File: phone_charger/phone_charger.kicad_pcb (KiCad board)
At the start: 2 copper layers, 19 parts, among them J1 Conn_01x02, J2 UE27AC54100, U1 ADP2302

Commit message: placed components
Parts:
- D1, D2, F1, R1, R3, R4, R5, R6, R7: moved to B.Cu
- moved J2 35.9 mm to (101.1, 57.0)
- moved J1 25.9 mm to (90.1, 79.1), turned to 180 degrees
- moved R7 25.7 mm to (101.2, 57.1)
- moved D1 25.6 mm to (90.6, 73.9), turned to 90 degrees
- moved D2 20.8 mm to (97.4, 79.2), turned to 90 degrees
- moved R4 19.2 mm to (104.1, 60.0)
- moved C3 18.8 mm to (93.9, 70.3), turned to 270 degrees
- moved R3 18.6 mm to (99.3, 60.0)
- moved C4 18.6 mm to (97.5, 70.3), turned to 270 degrees
- moved R5 18.2 mm to (101.2, 63.3)
- moved L1 14.7 mm to (104.8, 64.6)
- moved R1 14.0 mm to (90.6, 54.2), turned to 270 degrees
- moved R6 13.9 mm to (105.8, 63.2)
- moved R2 12.6 mm to (97.5, 82.5)
- moved F1 11.5 mm to (98.3, 72.7), turned to 180 degrees
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
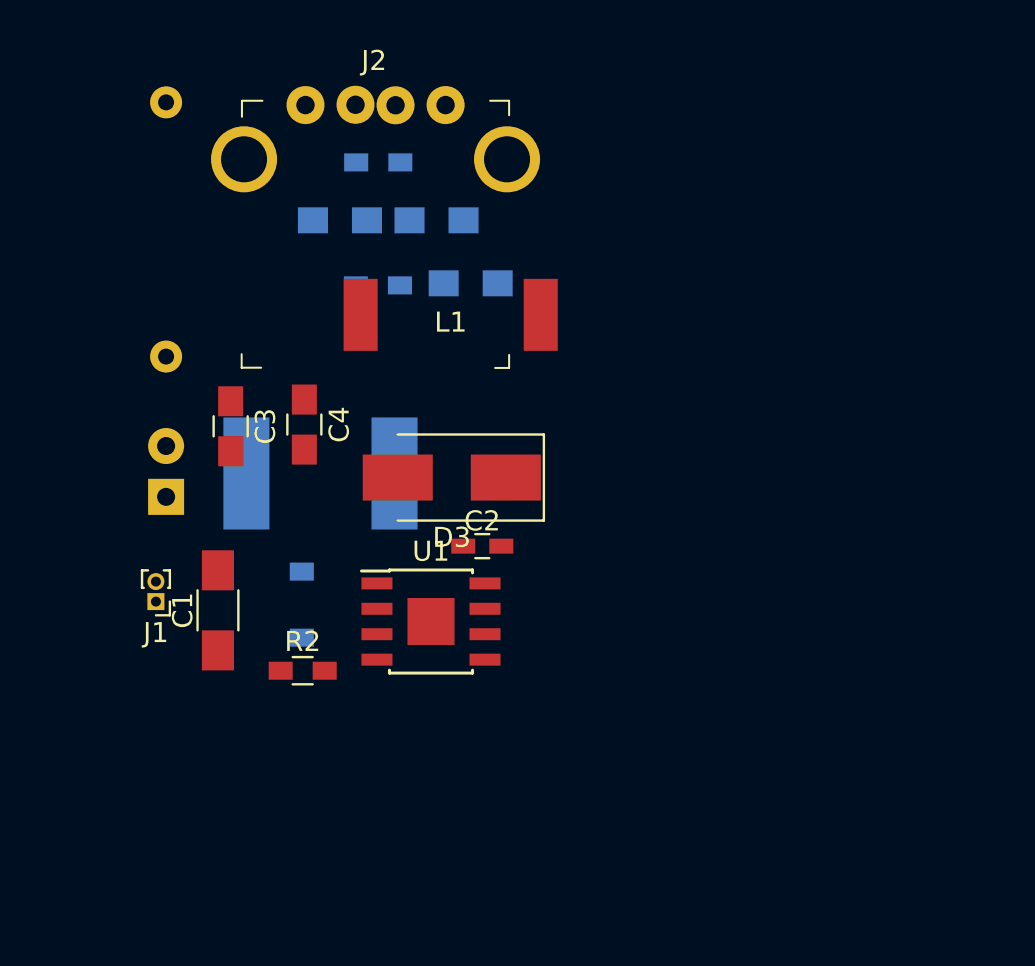
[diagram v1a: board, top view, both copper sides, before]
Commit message: laid out componenets onto charger board
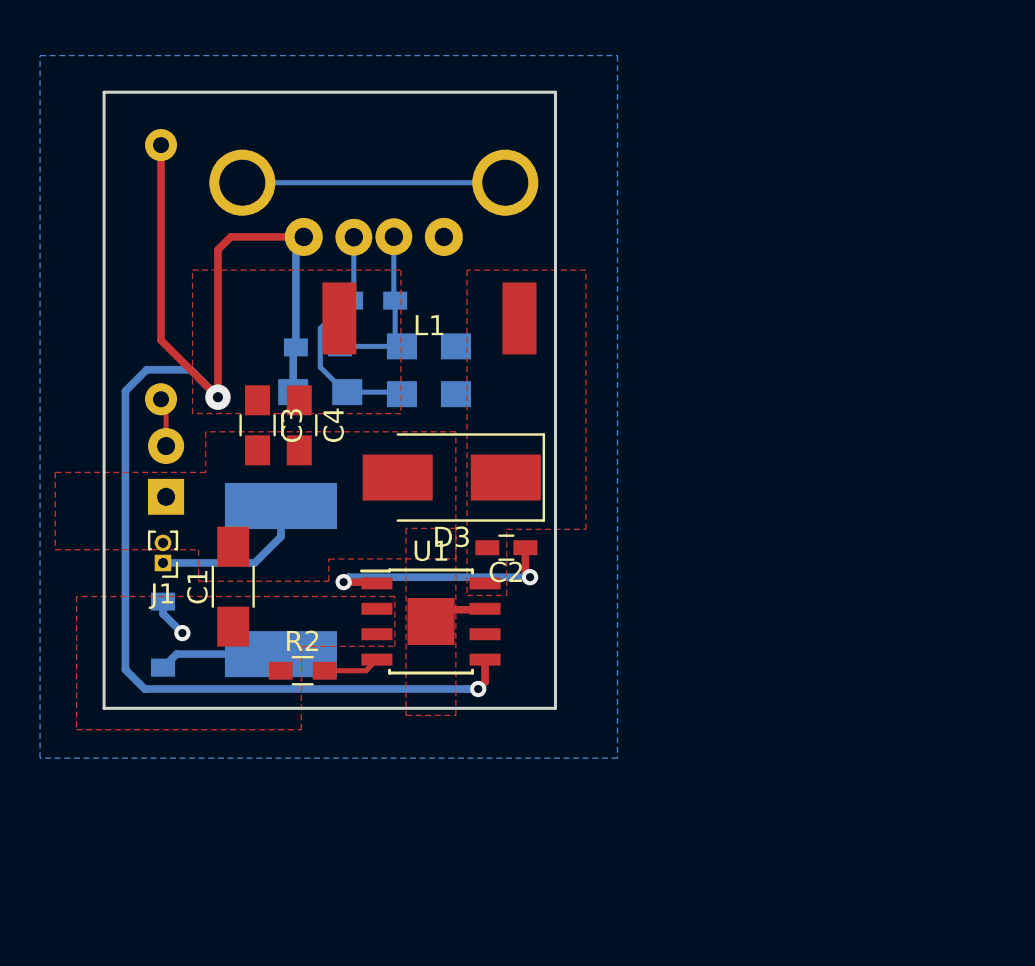
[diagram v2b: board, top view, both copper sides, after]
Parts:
- J2: moved to B.Cu
- moved R4 8.69 mm to (103.8, 68.7)
- moved R3 8.64 mm to (98.3, 68.6)
- moved D2 7.09 mm to (90.5, 80.7), turned to 270 degrees
- moved R7 6.91 mm to (101.0, 64.1)
- moved F1 5.68 mm to (96.4, 78.0), turned to 90 degrees
- moved R5 4.31 mm to (98.2, 66.4)
- moved R6 3.78 mm to (103.8, 66.3)
- moved R1 2.15 mm to (90.4, 56.3)
- moved J1 1.96 mm to (90.5, 77.2)
- moved C1 1.41 mm to (94.0, 78.4)
- moved C3 1.35 mm to (95.2, 70.3)
- moved C2 1.21 mm to (107.6, 76.4), turned to 180 degrees
- moved J2 1.17 mm to (101.0, 58.2)
- moved L1 1.08 mm to (103.8, 64.8)
- moved C4 0.26 mm to (97.3, 70.3)
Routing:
- net VBUS: track 0.00 -> 72.9 mm, vias 0 -> 2
- net Net-(J2-PadSH): track 0.00 -> 13.1 mm
- net Net-(C2-Pad1): track 0.00 -> 12.8 mm, vias 0 -> 2
- net /D-: track 0.00 -> 11.9 mm
- net /D+: track 0.00 -> 8.77 mm
- net Net-(F1-Pad2): track 0.00 -> 7.97 mm
- net EPAD: track 0.00 -> 6.26 mm
- net Net-(D2-Pad2): track 0.00 -> 6.17 mm
- net Net-(R2-Pad2): track 0.00 -> 2.84 mm
- net Net-(D1-Pad2): track 0.00 -> 2.44 mm
- net /reg_in: track 0.00 -> 1.97 mm, vias 0 -> 1
- added copper zone on F.Cu, net /reg_in
- added copper zone on B.Cu, net EPAD
- added copper zone on F.Cu, net EPAD
- added copper zone on F.Cu, net Net-(C2-Pad2)
- added copper zone on F.Cu, net VBUS
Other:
- board outline added: 22.6 x 30.8 mm
- net class Default: clearance 0.2 -> 0.1524; trace_width 0.25 -> 0.254; via_dia 0.8 -> 0.5588; via_drill 0.4 -> 0.254
- net class Power added: clearance 0.1524, trace_width 0.381, via_dia 0.8128, via_drill 0.4064
- rule trace_clearance: 0.2 -> 0.1524
- rule trace_min: 0.2 -> 0.1524
- rule via_min_drill: 0.3 -> 0.254
- rule via_min_size: 0.4 -> 0.5588

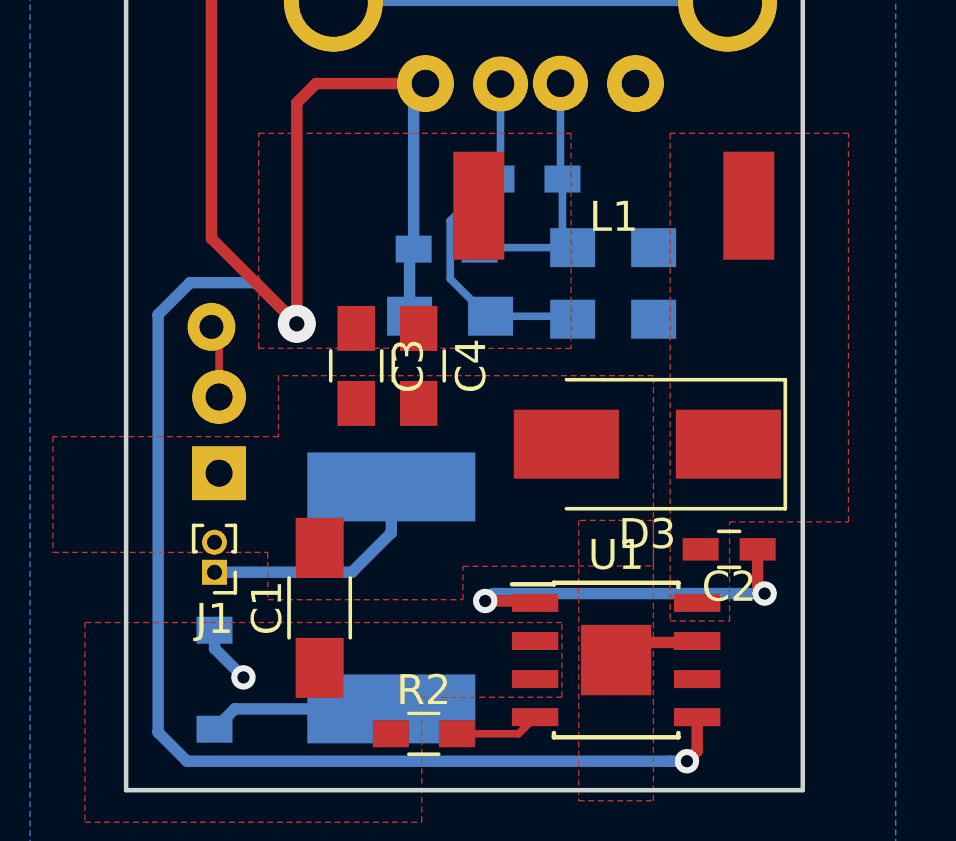
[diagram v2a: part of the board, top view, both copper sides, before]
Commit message: Updated silkscreen for phone charger
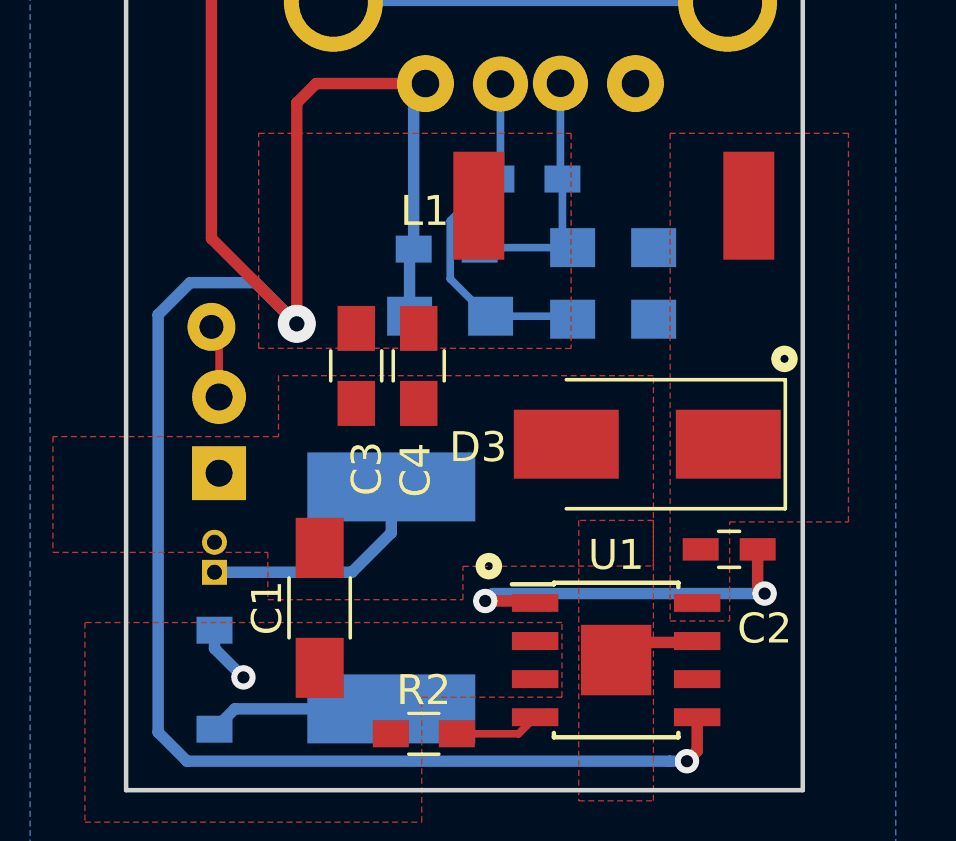
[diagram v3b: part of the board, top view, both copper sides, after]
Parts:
- D2: footprint Diodes_SMD:D_SOD-123 -> phone_charger:D_SOD-123
- J1: moved to B.Cu
- turned J1 to 0 degrees

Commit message: Update PCB
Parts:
- R1: footprint Resistors_THT:R_Axial_DIN0309_L9.0mm_D3.2mm_P12.70mm_Horizontal -> Resistor_THT:R_Axial_DIN0207_L6.3mm_D2.5mm_P10.16mm_Horizontal
- moved D1 17.7 mm to (91.4, 56.1), turned to 180 degrees
- moved R1 13.3 mm to (90.2, 69.6), turned to 90 degrees
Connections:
- J2 pad SH: Net-(J2-PadSH) -> EPAD
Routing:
- net Net-(J2-PadSH): track 13.1 -> 0.00 mm
- net VBUS: track 72.9 -> 62.4 mm
- net Net-(D1-Pad2): track 2.44 -> 3.83 mm

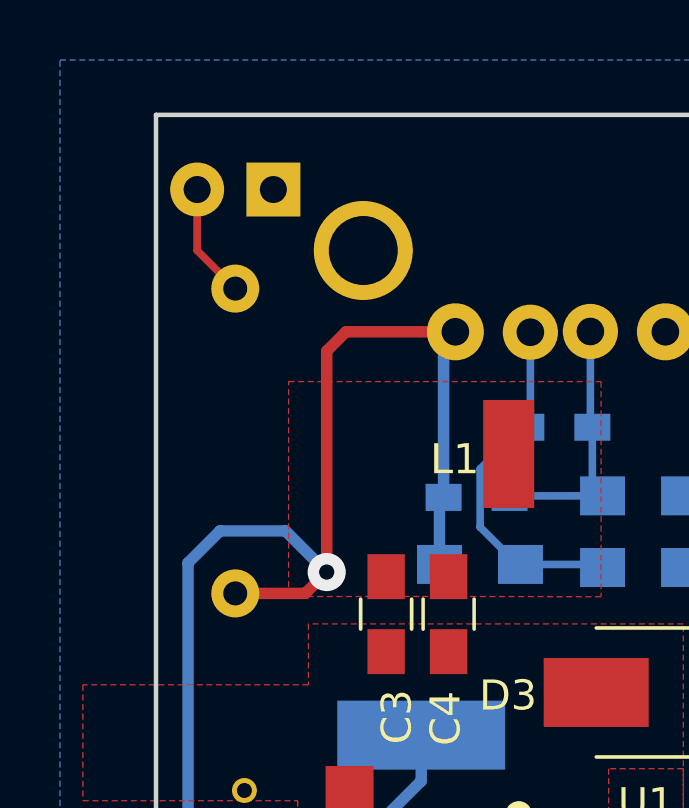
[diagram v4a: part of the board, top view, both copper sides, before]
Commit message: Fixed DRC error for phone charger
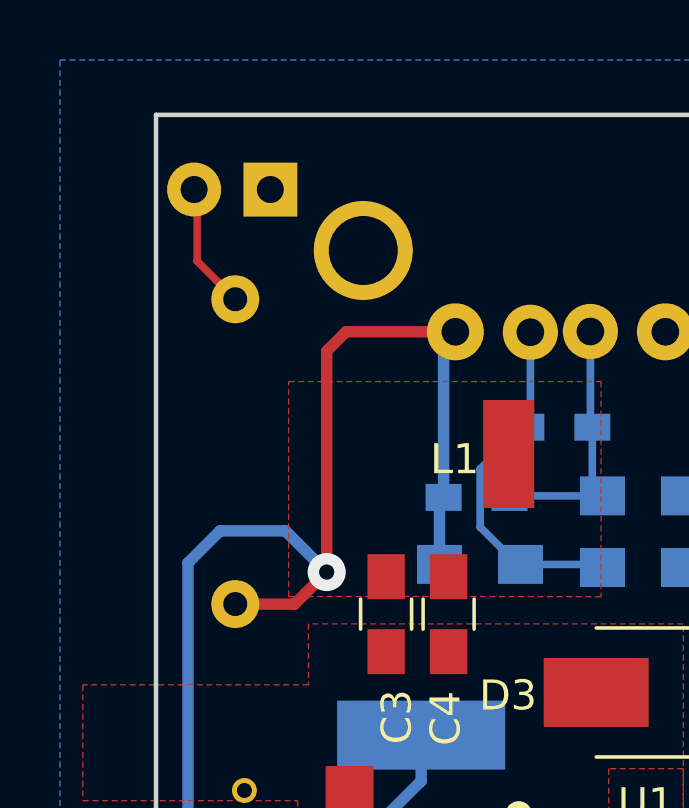
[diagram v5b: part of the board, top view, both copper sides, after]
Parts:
- moved R1 0.36 mm to (90.2, 70.0)
- moved D1 0.10 mm to (91.3, 56.1)
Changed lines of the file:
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@@
-(kicad_pcb (version 20171130) (host pcbnew 6.0.0-rc1-unknown)
+(kicad_pcb (version 20171130) (host pcbnew "(5.0.0-3-g5ebb6b6)")
   (general
     (thickness 1.6)
     (drawings 7)
-    (tracks 62)
+    (tracks 63)
     (zones 0)
     (modules 19)
@@
     (zone_45_only no)
     (trace_min 0.1524)
+    (segment_width 0.2)
+    (edge_width 0.15)
     (via_size 0.5588)
     (via_drill 0.254)
@@
     (uvia_min_size 0.2)
     (uvia_min_drill 0.1)
-    (edge_width 0.15)
-    (segment_width 0.2)
     (pcb_text_width 0.3)
     (pcb_text_size 1.5 1.5)
@@
     (uvia_dia 0.5588)
     (uvia_drill 0.254)
+    (diff_pair_gap 0.254)
     (diff_pair_width 0.254)
-    (diff_pair_gap 0.254)
     (add_net /D+)
     (add_net /D-)
@@
     (uvia_dia 0.5588)
     (uvia_drill 0.254)
+    (diff_pair_gap 0.254)
     (diff_pair_width 0.254)
-    (diff_pair_gap 0.254)
     (add_net /reg_in)
     (add_net EPAD)
@@
   )
   (module Resistor_THT:R_Axial_DIN0207_L6.3mm_D2.5mm_P10.16mm_Horizontal (layer B.Cu)
-    (at 90.17 69.596 90)
+    (at 90.17 69.9516 90)
     (descr "Resistor, Axial_DIN0207 series, Axial, Horizontal, pin pitch=10.16mm, 0.25W = 1/4W, length*diameter=6.3*2.5mm^2, http://cdn-reichelt.de/documents/datenblatt/B400/1_4W%23YAG.pdf")
     (tags "Resistor Axial_DIN0207 series Axial Horizontal pin pitch 10.16mm 0.25W = 1/4W length 6.3mm diameter 2.5mm")
@@
   )
   (module LEDs:LED_D3.0mm (layer B.Cu)
-    (at 91.44 56.134 180)
+    (at 91.3384 56.134 180)
     (descr "LED, diameter 3.0mm, 2 pins")
     (tags "LED diameter 3.0mm 2 pins")
@@
   (segment (start 91.8464 67.5132) (end 89.662 67.5132) (width 0.381) (layer B.Cu) (net 2))
   (segment (start 92.5068 69.596) (end 93.218 68.8848) (width 0.381) (layer F.Cu) (net 2))
-  (segment (start 90.17 69.596) (end 92.5068 69.596) (width 0.381) (layer F.Cu) (net 2))
-  (segment (start 88.9 58.166) (end 90.17 59.436) (width 0.254) (layer F.Cu) (net 3))
-  (segment (start 88.9 56.134) (end 88.9 58.166) (width 0.254) (layer F.Cu) (net 3))
+  (segment (start 92.1512 69.9516) (end 92.5068 69.596) (width 0.381) (layer F.Cu) (net 2))
+  (segment (start 90.17 69.9516) (end 92.1512 69.9516) (width 0.381) (layer F.Cu) (net 2))
+  (segment (start 88.9 58.5216) (end 90.17 59.7916) (width 0.254) (layer F.Cu) (net 3))
+  (segment (start 88.9 56.134) (end 88.9 58.5216) (width 0.254) (layer F.Cu) (net 3))
   (segment (start 100.0072 63.9244) (end 99.8728 64.0588) (width 0.254) (layer B.Cu) (net 4))
   (segment (start 100.0072 60.891) (end 100.0072 63.9244) (width 0.254) (layer B.Cu) (net 4))
